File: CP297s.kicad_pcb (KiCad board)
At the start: 2 copper layers, 155.1 x 156 mm, 127 parts, among them J1 Conn_01x05_Male, J2 Conn_01x04_Female, J3 pin header 01x15 2.54mm, J4 Conn_01x06_Female, J5 PG203J, J6 PG203J, J7 PG203J, K1 CONN_3, K2 CONN_3, K3 TK85_BUS, P2 CONN_2, P6 CONN_2, SW1 SW_SPDT, U1 Z80, U10 74LS125, U11 74LS393, U12 74LS574, U13 74LS08, U14 74LS251, U15 74HC86, U16 74LS245, U17 74LS32, U18 74HCT00, U19 74LS138, U2 62256, U20 74HC74, U21 74HC74, U22 74LS165, U23 74LS32, U24 AY-3-8910, U25 74LS08, U26 74LS138, U3 27256, U4 74HC04, U5 74HC74, U6 74LS393, U7 74LS11, U8 74LS32, U9 74LS245, X1 6.5MHz

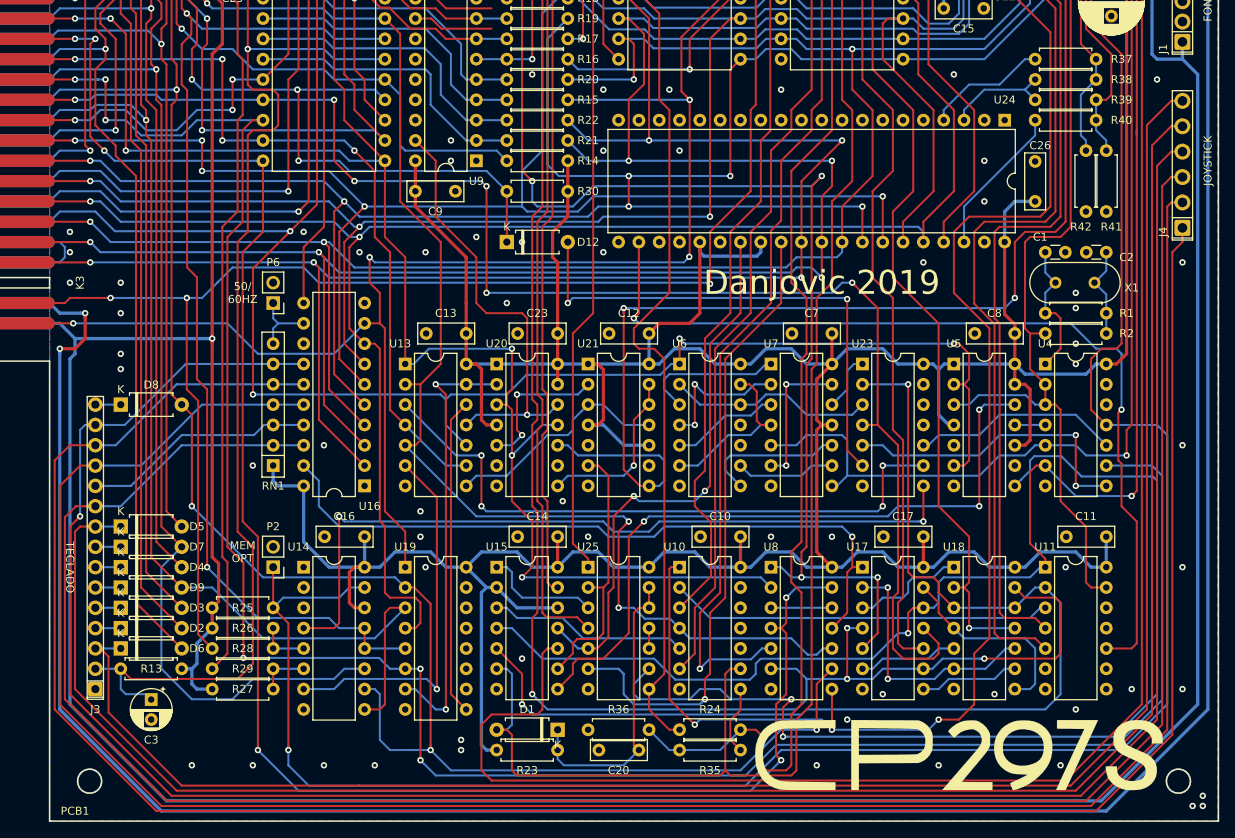
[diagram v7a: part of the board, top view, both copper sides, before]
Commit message: Added header for Tek V2
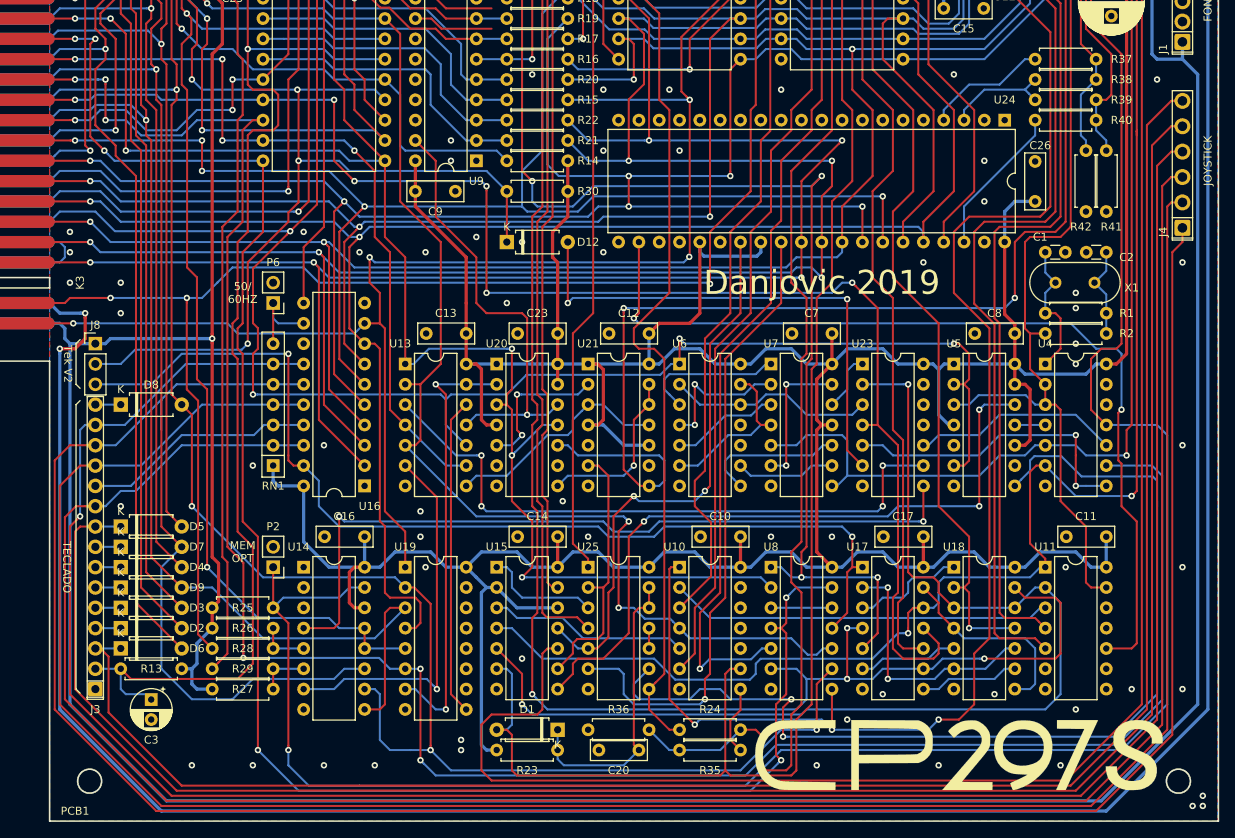
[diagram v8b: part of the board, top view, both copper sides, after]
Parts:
- added J8: Conn_01x03_Female, Connector_PinHeader_2.54mm:PinHeader_1x03_P2.54mm_Vertical, F.Cu at (31.1, 143.5)
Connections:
- U15 pad 9: /INVERT -> INVERT
- U26 pad 5: /~IOWR -> ~IOWR
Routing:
- net ~WAIT: track 104.0 -> 149.6 mm, vias 5 -> 6
- net ~KBD: track 89.6 -> 130.8 mm, vias 1 -> 2
- net Net-(J3-Pad13): track 279.0 -> 282.8 mm
- net Net-(P6-Pad1): track 8.78 -> 11.1 mm
- net D7': track 263.3 -> 261.2 mm
- net ~RESET: track 171.1 -> 171.6 mm
- net ~IORQ: track 214.8 -> 215.3 mm
- net 3.2M: track 225.4 -> 225.9 mm
- net GND: vias 89 -> 88
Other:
- board text added: "Tek V2"
